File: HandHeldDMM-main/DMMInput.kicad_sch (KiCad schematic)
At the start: 11 parts, among them J2 Conn_01x02, J5 Conn_01x02, J7 Conn_01x02

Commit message: PCB rev 1 with schematic change ideas
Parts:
- R10: footprint Resistor_THT:R_Axial_DIN0516_L15.5mm_D5.0mm_P7.62mm_Vertical -> Resistor_THT:R_Axial_DIN0516_L15.5mm_D5.0mm_P20.32mm_Horizontal
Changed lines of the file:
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@@
       (effects (font (size 1.27 1.27)))
     )
-    (property "Footprint" "Resistor_THT:R_Axial_DIN0516_L15.5mm_D5.0mm_P7.62mm_Vertical" (at 119.38 25.273 90)
+    (property "Footprint" "Resistor_THT:R_Axial_DIN0516_L15.5mm_D5.0mm_P20.32mm_Horizontal" (at 119.38 25.273 90)
       (effects (font (size 1.27 1.27)) hide)
     )

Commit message: Its going
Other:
- note added: "Change MOV values to new range number - # of MOVs depends on voltage rating of each selected Layout thoughts: - pcb slot surrounding MOVs / inbetween move traces - seperate MOVs to prevent arcing across"
- note added: "Thermister and PTC needed???? 10M res voltage rating"
- note removed: "- # of MOVs depends on voltage rating of each selected Layout thoughts: - pcb slot surrounding MOVs / inbetween move traces - seperate MOVs to prevent arcing across"
- note removed: "FIND SMALLER RES"
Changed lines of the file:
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@@
     (effects (font (size 1.27 1.27)) (justify left bottom))
   )
-  (text "FIND SMALLER RES" (at 105.41 18.415 0)
-    (effects (font (size 1.27 1.27)) (justify left bottom))
+  (text "Thermister and PTC needed????\n\n10M res voltage rating"
+    (at 95.25 5.715 0)
+    (effects (font (size 3 3) (thickness 0.6) bold) (justify left bottom))
   )
   (text "Lable with silk screen" (at 1.905 38.1 0)
@@
     (effects (font (size 1.27 1.27)) (justify left bottom))
   )
-  (text "- # of MOVs depends on voltage rating of each selected\n\nLayout thoughts:\n- pcb slot surrounding MOVs / inbetween move traces\n- seperate MOVs to prevent arcing across"
+  (text "Change MOV values to new range number\n\n\n- # of MOVs depends on voltage rating of each selected\n\nLayout thoughts:\n- pcb slot surrounding MOVs / inbetween move traces\n- seperate MOVs to prevent arcing across"
     (at 97.155 64.77 0)
     (effects (font (size 1 1)) (justify left bottom))

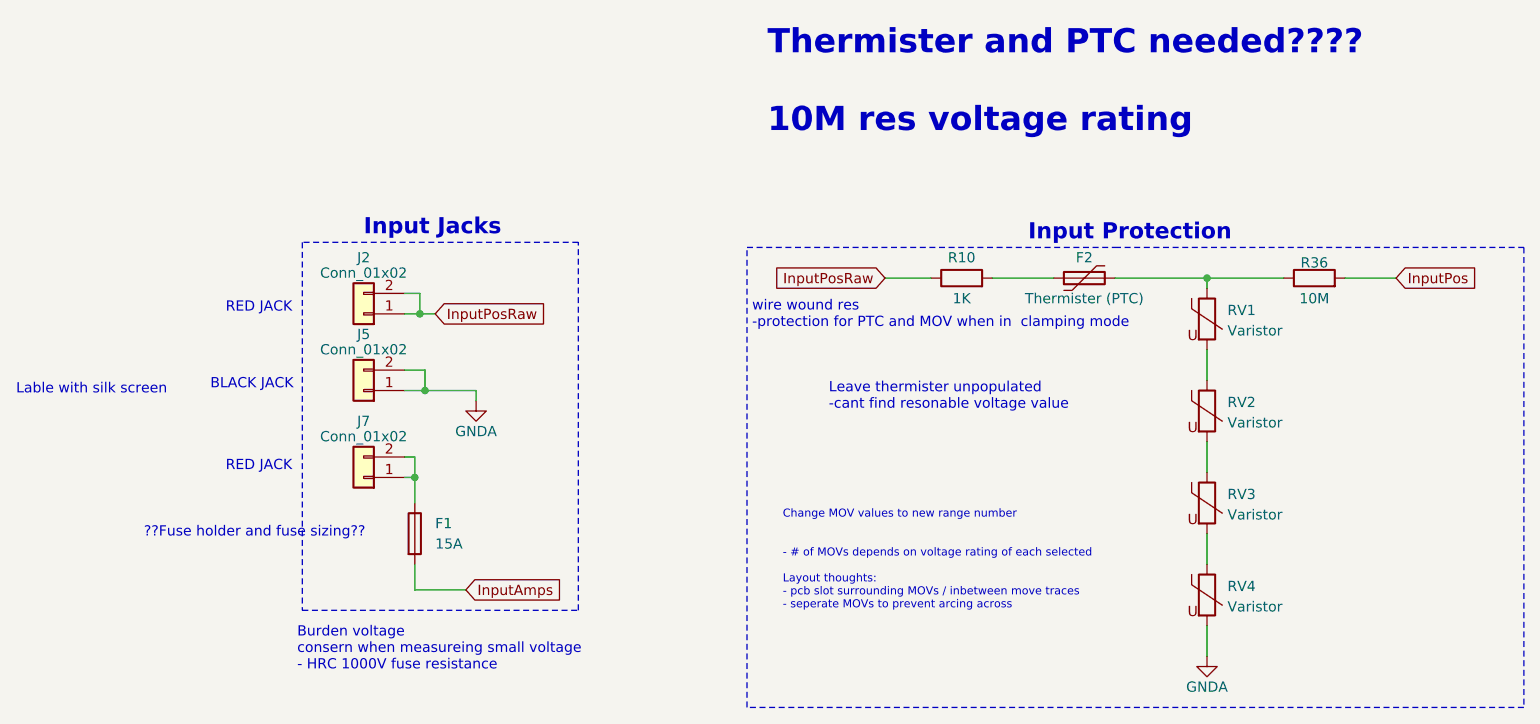
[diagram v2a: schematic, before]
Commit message: Layout / routing V2 with schematic fixes
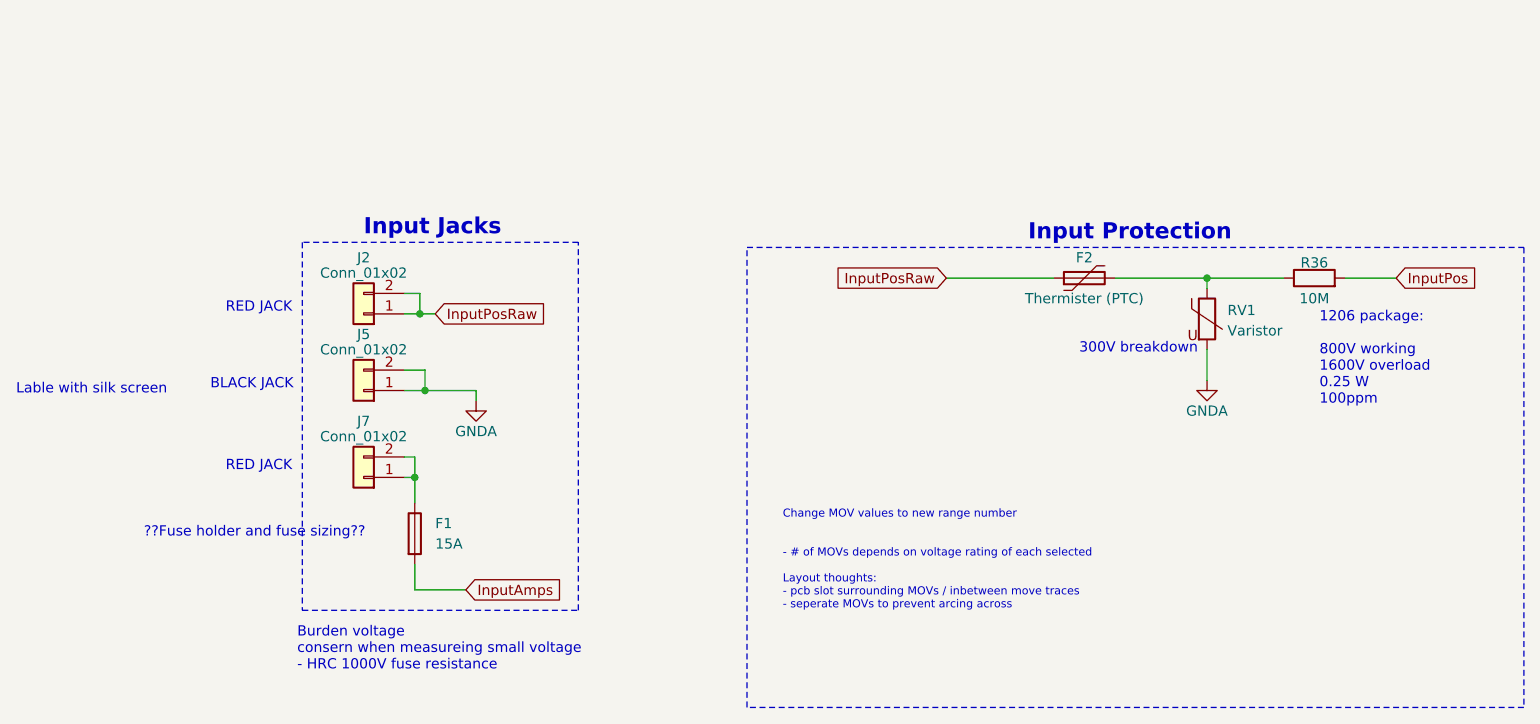
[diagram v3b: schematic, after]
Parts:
- removed R10: 1K, Resistor_THT:R_Axial_DIN0516_L15.5mm_D5.0mm_P20.32mm_Horizontal, symbol Device:R
- removed RV2, RV3, RV4: Varistor, Resistor_THT:R_Axial_DIN0207_L6.3mm_D2.5mm_P5.08mm_Vertical, symbol Device:Varistor
- F1: PART# (none) -> C3130; Price / 1 (none) -> 0.0174
- J2, J7: PART# (none) -> C7437321; Price / 1 (none) -> 0.9180
- J5: PART# (none) -> C7437322; Price / 1 (none) -> 0.9180
- R36: PART# (none) -> C2078785; Price / 1 (none) -> 0.29797
- RV1: PART# (none) -> C283925; Price / 1 (none) -> 0.0298
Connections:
- net GNDA: now also RV1.2
- net InputPosRaw: now also F2.1
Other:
- note added: "1206 package: 800V working 1600V overload 0.25 W 100ppm"
- note added: "300V breakdown"
- note removed: "Leave thermister unpopulated -cant find resonable voltage value"
- note removed: "Thermister and PTC needed???? 10M res voltage rating"
- note removed: "wire wound res -protection for PTC and MOV when in clamping mode"
